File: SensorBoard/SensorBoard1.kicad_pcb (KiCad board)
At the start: 2 copper layers, 39.4 x 66 mm, 101 parts, among them J1 Conn_01x04_Male, J2 Conn_01x02_Male, U1 JST4Pin, U2 JST4Pin, U3 JST4Pin

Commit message: updated sensor board worked on by olivia ??? changes made
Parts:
- moved U2 3.31 mm to (132.6, 95.0)
- moved U3 3.31 mm to (132.6, 110.2)
- moved U1 3.30 mm to (132.6, 80.0)
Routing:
- net GND: track 2.54 -> 177.8 mm
- net Net-(A1-Pad30): track 12.3 -> 66.7 mm
- net (no net): track 0.00 -> 21.1 mm
- net Net-(A1-Pad27): track 79.4 -> 85.3 mm
- net Net-(A1-Pad24): track 10.4 -> 8.48 mm
- net Net-(A1-Pad23): track 10.4 -> 8.64 mm
- net Net-(A1-Pad9): track 18.6 -> 17.2 mm
- net Net-(A1-Pad6): track 16.2 -> 15.1 mm
- net Net-(A1-Pad5): track 15.9 -> 15.0 mm
- net Net-(A1-Pad8): track 10.7 -> 11.3 mm
- net Net-(A1-Pad7): track 10.7 -> 11.3 mm
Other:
- board outline removed

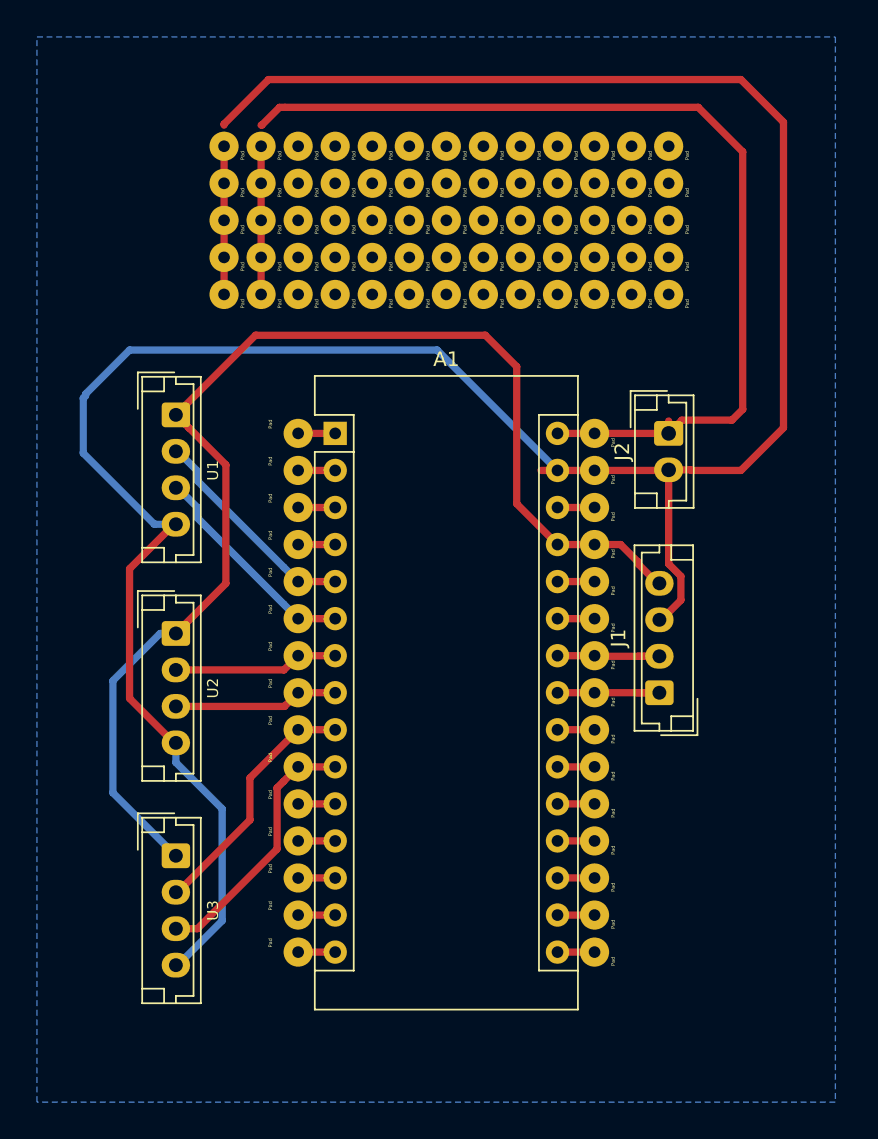
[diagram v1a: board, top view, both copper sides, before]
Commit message: switched pins on ultrasonic to PWM pins and switched some wiring
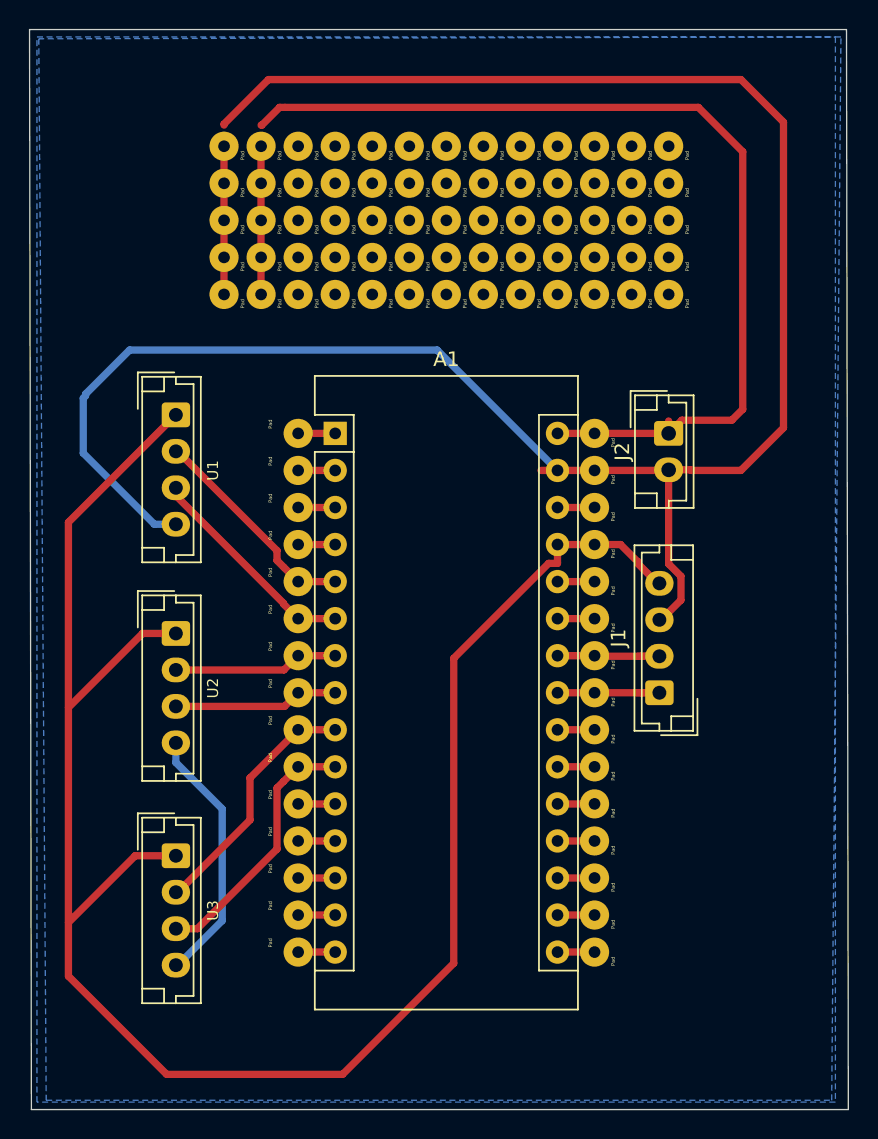
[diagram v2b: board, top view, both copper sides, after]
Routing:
- net Net-(A1-Pad27): track 85.3 -> 132.8 mm
- net GND: track 177.8 -> 160.3 mm
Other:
- board outline added: 56.1 x 74 mm
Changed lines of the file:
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@@
-(kicad_pcb (version 20171130) (host pcbnew "(5.1.4-0)")
+(kicad_pcb (version 20171130) (host pcbnew "(5.1.4)-1")
   (general
     (thickness 1.6)
-    (drawings 0)
+    (drawings 4)
     (tracks 136)
     (zones 0)
@@
   (layers
     (0 F.Cu signal)
-    (31 B.Cu signal)
+    (31 B.Cu signal hide)
     (32 B.Adhes user)
     (33 F.Adhes user)
@@
     (42 Eco1.User user)
     (43 Eco2.User user)
-    (44 Edge.Cuts user hide)
+    (44 Edge.Cuts user)
     (45 Margin user)
     (46 B.CrtYd user)
@@
   )
   (setup
-    (last_trace_width 0.25)
+    (last_trace_width 0.5)
     (user_trace_width 0.5)
     (trace_clearance 0.2)
@@
     )
   )
+  (gr_line (start 178.562 53.594) (end 122.555 53.594) (layer Edge.Cuts) (width 0.05))
+  (gr_line (start 178.689 127.635) (end 178.562 53.594) (layer Edge.Cuts) (width 0.05))
+  (gr_line (start 122.682 127.635) (end 178.689 127.635) (layer Edge.Cuts) (width 0.05))
+  (gr_line (start 122.555 53.594) (end 122.682 127.635) (layer Edge.Cuts) (width 0.05))
   (segment (start 135.89 61.595) (end 135.89 64.135) (width 0.5) (layer F.Cu) (net 0))
   (segment (start 135.89 64.135) (end 135.89 66.675) (width 0.5) (layer F.Cu) (net 0))
@@
   (segment (start 135.89 60.145509) (end 135.89 60.071) (width 0.5) (layer F.Cu) (net 5))
   (segment (start 132.588 87.51) (end 132.463 87.51) (width 0.5) (layer F.Cu) (net 5))
-  (segment (start 132.463 87.51) (end 129.413 90.56) (width 0.5) (layer F.Cu) (net 5))
   (segment (start 132.463 102.496) (end 132.588 102.496) (width 0.5) (layer F.Cu) (net 5))
-  (segment (start 129.413 99.446) (end 132.463 102.496) (width 0.5) (layer F.Cu) (net 5))
-  (segment (start 129.413 90.56) (end 129.413 99.446) (width 0.5) (layer F.Cu) (net 5))
   (segment (start 140.97 111.76) (end 143.51 111.76) (width 0.5) (layer F.Cu) (net 6))
   (segment (start 161.29 86.36) (end 158.75 86.36) (width 0.5) (layer F.Cu) (net 7))
@@
   (segment (start 164.26 90.085) (end 164.26 90.21) (width 0.5) (layer F.Cu) (net 9))
   (segment (start 161.29 88.9) (end 163.075 88.9) (width 0.5) (layer F.Cu) (net 9))
-  (segment (start 133.486372 80.908372) (end 132.588 80.01) (width 0.5) (layer F.Cu) (net 9))
-  (segment (start 136.017 83.439) (end 133.486372 80.908372) (width 0.5) (layer F.Cu) (net 9))
-  (segment (start 136.017 91.567) (end 136.017 83.439) (width 0.5) (layer F.Cu) (net 9))
-  (segment (start 132.588 94.996) (end 136.017 91.567) (width 0.5) (layer F.Cu) (net 9))
-  (segment (start 155.956 86.106) (end 155.956 76.708) (width 0.5) (layer F.Cu) (net 9))
-  (segment (start 158.75 88.9) (end 155.956 86.106) (width 0.5) (layer F.Cu) (net 9))
-  (segment (start 155.956 76.708) (end 153.797 74.549) (width 0.5) (layer F.Cu) (net 9))
-  (segment (start 138.049 74.549) (end 132.588 80.01) (width 0.5) (layer F.Cu) (net 9))
-  (segment (start 153.797 74.549) (end 138.049 74.549) (width 0.5) (layer F.Cu) (net 9))
-  (segment (start 131.513 94.996) (end 128.27 98.239) (width 0.5) (layer B.Cu) (net 9))
-  (segment (start 132.588 94.996) (end 131.513 94.996) (width 0.5) (layer B.Cu) (net 9))
-  (segment (start 128.27 105.918) (end 132.588 110.236) (width 0.5) (layer B.Cu) (net 9))
-  (segment (start 128.27 98.239) (end 128.27 105.918) (width 0.5) (layer B.Cu) (net 9))
+  (segment (start 158.149999 90.189999) (end 151.638 96.701998) (width 0.5) (layer F.Cu) (net 9))
+  (segment (start 158.75 88.9) (end 158.75 90.189999) (width 0.5) (layer F.Cu) (net 9))
+  (segment (start 158.75 90.189999) (end 158.149999 90.189999) (width 0.5) (layer F.Cu) (net 9))
+  (segment (start 151.638 96.701998) (end 151.638 117.602) (width 0.5) (layer F.Cu) (net 9))
+  (segment (start 151.638 117.602) (end 144.018 125.222) (width 0.5) (layer F.Cu) (net 9))
+  (segment (start 144.018 125.222) (end 131.953 125.222) (width 0.5) (layer F.Cu) (net 9))
+  (segment (start 131.953 125.222) (end 125.222 118.491) (width 0.5) (layer F.Cu) (net 9))
+  (segment (start 125.222 87.376) (end 132.588 80.01) (width 0.5) (layer F.Cu) (net 9))
+  (segment (start 129.794 110.236) (end 125.222 114.808) (width 0.5) (layer F.Cu) (net 9))
+  (segment (start 132.588 110.236) (end 129.794 110.236) (width 0.5) (layer F.Cu) (net 9))
+  (segment (start 125.222 118.491) (end 125.222 114.808) (width 0.5) (layer F.Cu) (net 9))
+  (segment (start 130.302 94.996) (end 125.222 100.076) (width 0.5) (layer F.Cu) (net 9))
+  (segment (start 132.588 94.996) (end 130.302 94.996) (width 0.5) (layer F.Cu) (net 9))
+  (segment (start 125.222 114.808) (end 125.222 100.076) (width 0.5) (layer F.Cu) (net 9))
+  (segment (start 125.222 100.076) (end 125.222 87.376) (width 0.5) (layer F.Cu) (net 9))
   (segment (start 140.97 106.68) (end 143.51 106.68) (width 0.5) (layer F.Cu) (net 10))
   (segment (start 161.29 91.44) (end 158.75 91.44) (width 0.5) (layer F.Cu) (net 11))
@@
   (segment (start 158.75 101.6) (end 161.29 101.6) (width 0.5) (layer F.Cu) (net 19))
   (segment (start 140.97 93.98) (end 143.51 93.98) (width 0.5) (layer F.Cu) (net 20))
-  (segment (start 134.063 86.36) (end 134.063 87.073) (width 0.5) (layer B.Cu) (net 20))
-  (segment (start 134.063 87.073) (end 139.970511 92.980511) (width 0.5) (layer B.Cu) (net 20))
-  (segment (start 132.713 85.01) (end 134.063 86.36) (width 0.5) (layer B.Cu) (net 20))
-  (segment (start 139.970511 92.980511) (end 140.97 93.98) (width 0.5) (layer B.Cu) (net 20))
   (segment (start 132.588 85.01) (end 132.713 85.01) (width 0.5) (layer B.Cu) (net 20))
+  (segment (start 139.970511 92.980511) (end 140.97 93.98) (width 0.5) (layer F.Cu) (net 20))
+  (segment (start 139.970511 92.92902) (end 139.970511 92.980511) (width 0.5) (layer F.Cu) (net 20))
+  (segment (start 132.588 85.546509) (end 139.970511 92.92902) (width 0.5) (layer F.Cu) (net 20))
+  (segment (start 132.588 85.01) (end 132.588 85.546509) (width 0.5) (layer F.Cu) (net 20))
   (segment (start 158.75 104.14) (end 161.29 104.14) (width 0.5) (layer F.Cu) (net 21))
   (segment (start 140.97 91.44) (end 143.51 91.44) (width 0.5) (layer F.Cu) (net 22))
-  (segment (start 134.063 84.533) (end 139.970511 90.440511) (width 0.5) (layer B.Cu) (net 22))
-  (segment (start 134.063 83.86) (end 134.063 84.533) (width 0.5) (layer B.Cu) (net 22))
-  (segment (start 139.970511 90.440511) (end 140.97 91.44) (width 0.5) (layer B.Cu) (net 22))
-  (segment (start 132.713 82.51) (end 134.063 83.86) (width 0.5) (layer B.Cu) (net 22))
   (segment (start 132.588 82.51) (end 132.713 82.51) (width 0.5) (layer B.Cu) (net 22))
+  (segment (start 139.970511 90.440511) (end 140.97 91.44) (width 0.5) (layer F.Cu) (net 22))
+  (segment (start 139.520509 89.990509) (end 139.970511 90.440511) (width 0.5) (layer F.Cu) (net 22))
+  (segment (start 139.520509 89.317509) (end 139.520509 89.990509) (width 0.5) (layer F.Cu) (net 22))
+  (segment (start 132.713 82.51) (end 139.520509 89.317509) (width 0.5) (layer F.Cu) (net 22))
+  (segment (start 132.588 82.51) (end 132.713 82.51) (width 0.5) (layer F.Cu) (net 22))
   (segment (start 158.75 106.68) (end 161.29 106.68) (width 0.5) (layer F.Cu) (net 23))
   (segment (start 140.97 88.9) (end 143.51 88.9) (width 0.5) (layer F.Cu) (net 24))
@@
     )
   )
-  (zone (net 0) (net_name "") (layer Edge.Cuts) (hatch edge 0.508)
+  (zone (net 5) (net_name GND) (layer B.Cu) (hatch edge 0.508)
     (connect_pads (clearance 0.508))
     (min_thickness 0.254)
@@
     (polygon
       (pts
-        (xy 179.324 52.959) (xy 122.047 52.959) (xy 122.047 128.143) (xy 179.07 128.143) (xy 179.07 52.959)
-        (xy 179.197 52.959) (xy 179.07 53.086)
+        (xy 123.698 127) (xy 177.546 127) (xy 178.181 54.102) (xy 123.19 54.229)
       )
     )
